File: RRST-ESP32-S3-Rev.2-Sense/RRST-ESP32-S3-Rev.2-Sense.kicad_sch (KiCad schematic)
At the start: 35 parts, among them J1 USB_C_Receptacle_USB2.0_16P, J4 Conn_01x05_Socket, J5 Conn_01x02_Socket, J6 Conn_01x02_Socket, SW1 SW_Push, SW2 SW_Push, U1 LD1117S33TR_SOT223, U2 ESP32-S3-WROOM-1, U3 MCP2561-E-SN

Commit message: 自動配線前
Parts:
- removed CAN_BUS1, CAN_BUS2: Conn_01x04_Socket, Connector_JST:JST_GH_SM04B-GHS-TB_1x04-1MP_P1.25mm_Horizontal, symbol Connector:Conn_01x04_Socket
- removed J4: Conn_01x05_Socket, Connector_PinSocket_2.54mm:PinSocket_1x05_P2.54mm_Horizontal, symbol Connector:Conn_01x05_Socket
- removed J5, J6: Conn_01x02_Socket, Connector_JST:JST_PH_S2B-PH-K_1x02_P2.00mm_Horizontal, symbol Connector:Conn_01x02_Socket
- removed U3: MCP2561-E-SN, Package_SO:SOIC-8_3.9x4.9mm_P1.27mm, symbol Interface_CAN_LIN:MCP2561-E-SN
- added J1, J3: Conn_01x22_Pin, Connector_PinHeader_2.54mm:PinHeader_1x22_P2.54mm_Vertical, symbol Connector:Conn_01x22_Pin
- added J5, J6: Conn_01x04_Socket, Connector_JST:JST_XH_B4B-XH-A_1x04_P2.50mm_Vertical, symbol Connector:Conn_01x04_Socket
- added U4: MCP2561-E-SN, Package_SO:SOIC-8_3.9x4.9mm_P1.27mm, symbol Interface_CAN_LIN:MCP2561-E-SN
- R8: footprint Resistor_SMD:R_0603_1608Metric -> Resistor_SMD:R_0805_2012Metric
- renumbered C4 to C1, C7 to C2, C8 to C3, C9 to C4, C3 to C5, C2 to C7, C5 to C8, C1 to C9, D7 to D1, D1 to D2, D2 to D3, D3 to D4, D4 to D5, D5 to D6, D6 to D8, J1 to J2, R2 to R1, R3 to R2, R4 to R3, R5 to R4, R1 to R5, U2 to U1, U1 to U2
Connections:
- net IO2 is gone; now on net CAN_TX: U1.38 (IO2)
- net IO3 is gone; now on net CAN_RX: U1.15 (IO3)
- net +3.3V: now also J1.1 (Pin_1), J1.2 (Pin_2)
- net +5V: now also J1.21 (Pin_21), J5.1 (Pin_1), J6.1 (Pin_1)
- net 5V0: now also U4.3 (VDD)
- net CANH: now also U4.7 (CANH)
- net CANL: now also U4.6 (CANL)
- net CAN_RX: now also J1.13 (Pin_13), J5.4 (Pin_4), J6.4 (Pin_4), U4.4 (RXD)
- net CAN_TX: now also J3.5 (Pin_5), J5.3 (Pin_3), J6.3 (Pin_3), U4.1 (TXD)
- net DN: now also J3.20 (Pin_20)
- net DP: now also J3.19 (Pin_19)
- net EN: now also J1.3 (Pin_3)
- net GND: now also J1.22 (Pin_22), J3.1 (Pin_1), J3.21 (Pin_21), J3.22 (Pin_22), J5.2 (Pin_2), J6.2 (Pin_2), U4.2 (VSS), U4.8 (STBY)
- net IO0: now also J3.14 (Pin_14)
- net IO1: now also J3.4 (Pin_4)
- net IO10: now also J1.16 (Pin_16)
- net IO11: now also J1.17 (Pin_17)
- net IO12: now also J1.18 (Pin_18)
- net IO13: now also J1.19 (Pin_19)
- net IO14: now also J1.20 (Pin_20)
- net IO15: now also J1.8 (Pin_8)
- net IO16: now also J1.9 (Pin_9)
- net IO17: now also J1.10 (Pin_10)
- net IO18: now also J1.11 (Pin_11)
- net IO21: now also J3.18 (Pin_18)
- net IO35: now also J3.13 (Pin_13)
- net IO36: now also J3.12 (Pin_12)
- net IO37: now also J3.11 (Pin_11)
- net IO38: now also J3.10 (Pin_10)
- net IO39: now also J3.9 (Pin_9)
- net IO4: now also J1.4 (Pin_4)
- net IO40: now also J3.8 (Pin_8)
- net IO41: now also J3.7 (Pin_7)
- net IO42: now also J3.6 (Pin_6)
- net IO45: now also J3.15 (Pin_15)
- net IO46: now also J1.14 (Pin_14)
- net IO47: now also J3.17 (Pin_17)
- net IO48: now also J3.16 (Pin_16)
- net IO5: now also J1.5 (Pin_5)
- net IO6: now also J1.6 (Pin_6)
- net IO7: now also J1.7 (Pin_7)
- net IO8: now also J1.12 (Pin_12)
- net IO9: now also J1.15 (Pin_15)
- net RXD0: now also J3.3 (Pin_3)
- net TXD0: now also J3.2 (Pin_2)
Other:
- note removed: "ピン割り当て"

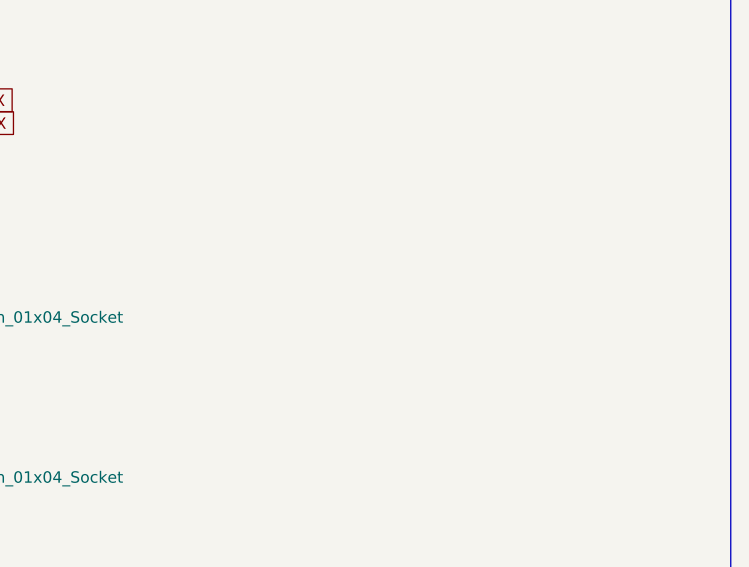
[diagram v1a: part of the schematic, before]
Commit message: 自動配線&未配線の手直し完了
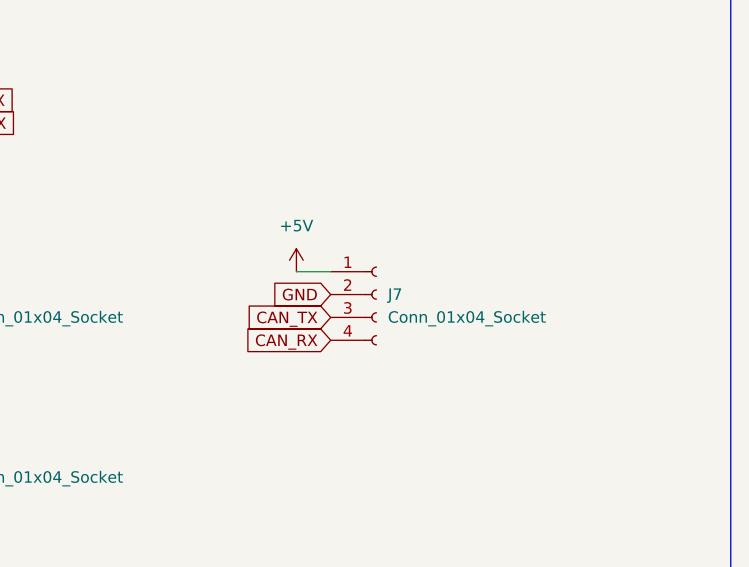
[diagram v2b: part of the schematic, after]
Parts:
- added J7: Conn_01x04_Socket, Connector_PinHeader_2.54mm:PinHeader_1x04_P2.54mm_Vertical, symbol Connector:Conn_01x04_Socket
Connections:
- net +5V: now also J7.1 (Pin_1)
- net CAN_RX: now also J7.4 (Pin_4)
- net CAN_TX: now also J7.3 (Pin_3)
- net GND: now also J7.2 (Pin_2)
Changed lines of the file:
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@@
 	(wire
 		(pts
+			(xy 332.74 128.27) (xy 336.55 128.27)
+		)
+		(stroke
+			(width 0)
+			(type default)
+		)
+	)
+	(wire
+		(pts
 			(xy 31.75 157.48) (xy 36.83 157.48)
 		)
@@
 		)
 	)
+	(global_label "CAN_RX"
+		(shape input)
+		(at 336.55 135.89 180)
+		(fields_autoplaced yes)
+		(effects
+			(font
+				(size 1.27 1.27)
+			)
+			(justify right)
+		)
+		(property "Intersheetrefs" "${INTERSHEET_REFS}"
+			(at 326.4286 135.89 0)
+			(hide yes)
+			(show_name no)
+			(do_not_autoplace no)
+			(effects
+				(font
+					(size 1.27 1.27)
+				)
+				(justify right)
+			)
+		)
+	)
 	(global_label "CANH"
 		(shape input)
@@
 		)
 	)
+	(global_label "GND"
+		(shape input)
+		(at 336.55 130.81 180)
+		(fields_autoplaced yes)
+		(effects
+			(font
+				(size 1.27 1.27)
+			)
+			(justify right)
+		)
+		(property "Intersheetrefs" "${INTERSHEET_REFS}"
+			(at 329.6943 130.81 0)
+			(hide yes)
+			(show_name no)
+			(do_not_autoplace no)
+			(effects
+				(font
+					(size 1.27 1.27)
+				)
+				(justify right)
+			)
+		)
+	)
 	(global_label "EN"
 		(shape input)
@@
 		)
 	)
+	(global_label "CAN_TX"
+		(shape input)
+		(at 336.55 133.35 180)
+		(fields_autoplaced yes)
+		(effects
+			(font
+				(size 1.27 1.27)
+			)
+			(justify right)
+		)
+		(property "Intersheetrefs" "${INTERSHEET_REFS}"
+			(at 326.731 133.35 0)
+			(hide yes)
+			(show_name no)
+			(do_not_autoplace no)
+			(effects
+				(font
+					(size 1.27 1.27)
+				)
+				(justify right)
+			)
+		)
+	)
 	(global_label "IO38"
 		(shape input)
@@
 	)
 	(symbol
+		(lib_id "power:+5V")
+		(at 332.74 128.27 0)
+		(unit 1)
+		(body_style 1)
+		(exclude_from_sim no)
+		(in_bom yes)
+		(on_board yes)
+		(in_pos_files yes)
+		(dnp no)
+		(fields_autoplaced yes)
+		(property "Reference" "#PWR026"
+			(at 332.74 132.08 0)
+			(hide yes)
+			(show_name no)
+			(do_not_autoplace no)
+			(effects
+				(font
+					(size 1.27 1.27)
+				)
+			)
+		)
+		(property "Value" "+5V"
+			(at 332.74 123.19 0)
+			(show_name no)
+			(do_not_autoplace no)
+			(effects
+				(font
+					(size 1.27 1.27)
+				)
+			)
+		)
+		(property "Footprint" ""
+			(at 332.74 128.27 0)
+			(hide yes)
+			(show_name no)
+			(do_not_autoplace no)
+			(effects
+				(font
+					(size 1.27 1.27)
+				)
+			)
+		)
+		(property "Datasheet" ""
+			(at 332.74 128.27 0)
+			(hide yes)
+			(show_name no)
+			(do_not_autoplace no)
+			(effects
+				(font
+					(size 1.27 1.27)
+				)
+			)
+		)
+		(property "Description" "Power symbol creates a global label with name \"+5V\""
+			(at 332.74 128.27 0)
+			(hide yes)
+			(show_name no)
+			(do_not_autoplace no)
+			(effects
+				(font
+					(size 1.27 1.27)
+				)
+			)
+		)
+		(pin "1"
+		)
+		(instances
+			(project "RRST-ESP32-S3-Rev.2-Sense"
+				(path "/08e3d388-f335-4566-99a5-7a0a51e9e065"
+					(reference "#PWR026")
+					(unit 1)
+				)
+			)
+		)
+	)
+	(symbol
 		(lib_id "Device:R")
 		(at 340.36 68.58 0)
@@
 					(unit 1)
 				)
+			)
+		)
+	)
+	(symbol
+		(lib_id "Connector:Conn_01x04_Socket")
+		(at 341.63 130.81 0)
+		(unit 1)
+		(body_style 1)
+		(exclude_from_sim no)
+		(in_bom yes)
+		(on_board yes)
+		(in_pos_files yes)
+		(dnp no)
+		(fields_autoplaced yes)
+		(property "Reference" "J7"
+			(at 342.9 130.8099 0)
+			(show_name no)
+			(do_not_autoplace no)
+			(effects
+				(font
+					(size 1.27 1.27)
+				)
+				(justify left)
+			)
+		)
+		(property "Value" "Conn_01x04_Socket"
+			(at 342.9 133.3499 0)
+			(show_name no)
+			(do_not_autoplace no)
+			(effects
+				(font
+					(size 1.27 1.27)
+				)
+				(justify left)
+			)
+		)
+		(property "Footprint" "Connector_PinHeader_2.54mm:PinHeader_1x04_P2.54mm_Vertical"
+			(at 341.63 130.81 0)
+			(hide yes)
+			(show_name no)
+			(do_not_autoplace no)
+			(effects
+				(font
+					(size 1.27 1.27)
+				)
+			)
+		)
+		(property "Datasheet" ""
+			(at 341.63 130.81 0)
+			(hide yes)
+			(show_name no)
+			(do_not_autoplace no)
+			(effects
+				(font
+					(size 1.27 1.27)
+				)
+			)
+		)
+		(property "Description" "Generic connector, single row, 01x04, script generated"
+			(at 341.63 130.81 0)
+			(hide yes)
+			(show_name no)
+			(do_not_autoplace no)
+			(effects
+				(font
+					(size 1.27 1.27)
+				)
+			)
+		)
+		(pin "1"
+		)
+		(pin "4"
+		)
+		(pin "3"
+		)
+		(pin "2"
+		)
+		(instances
+			(project "RRST-ESP32-S3-Rev.2-Sense"
+				(path "/08e3d388-f335-4566-99a5-7a0a51e9e065"
+					(reference "J7")
+					(unit 1)
+				)

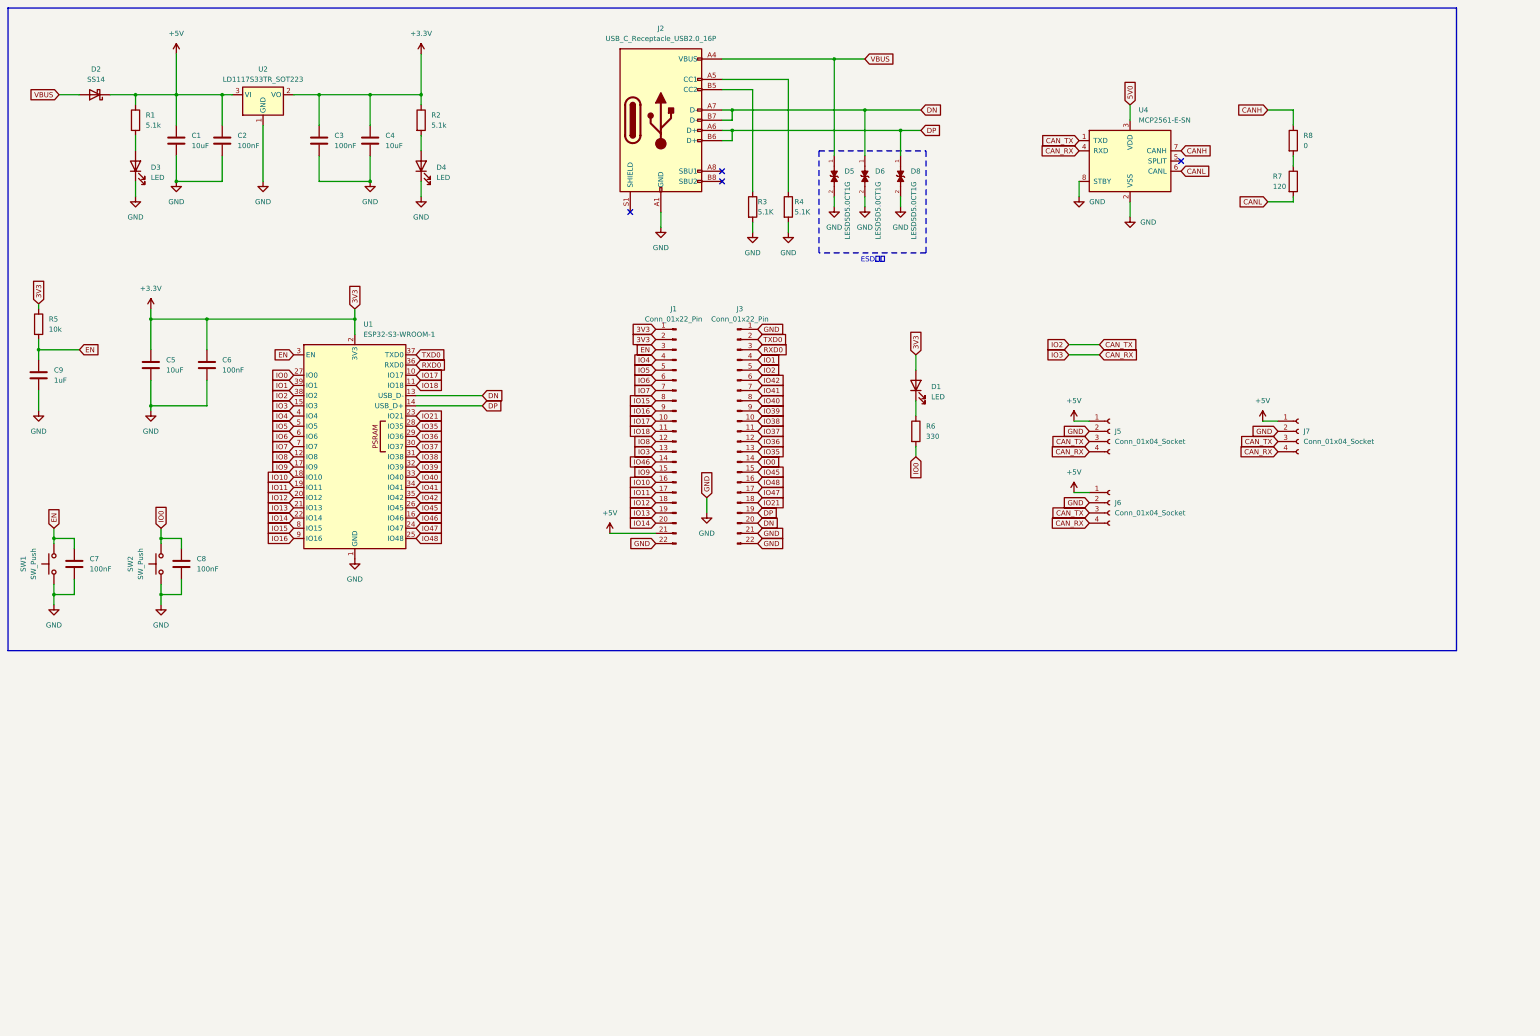
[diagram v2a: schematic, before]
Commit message: マイコンにセンサ入力を増設
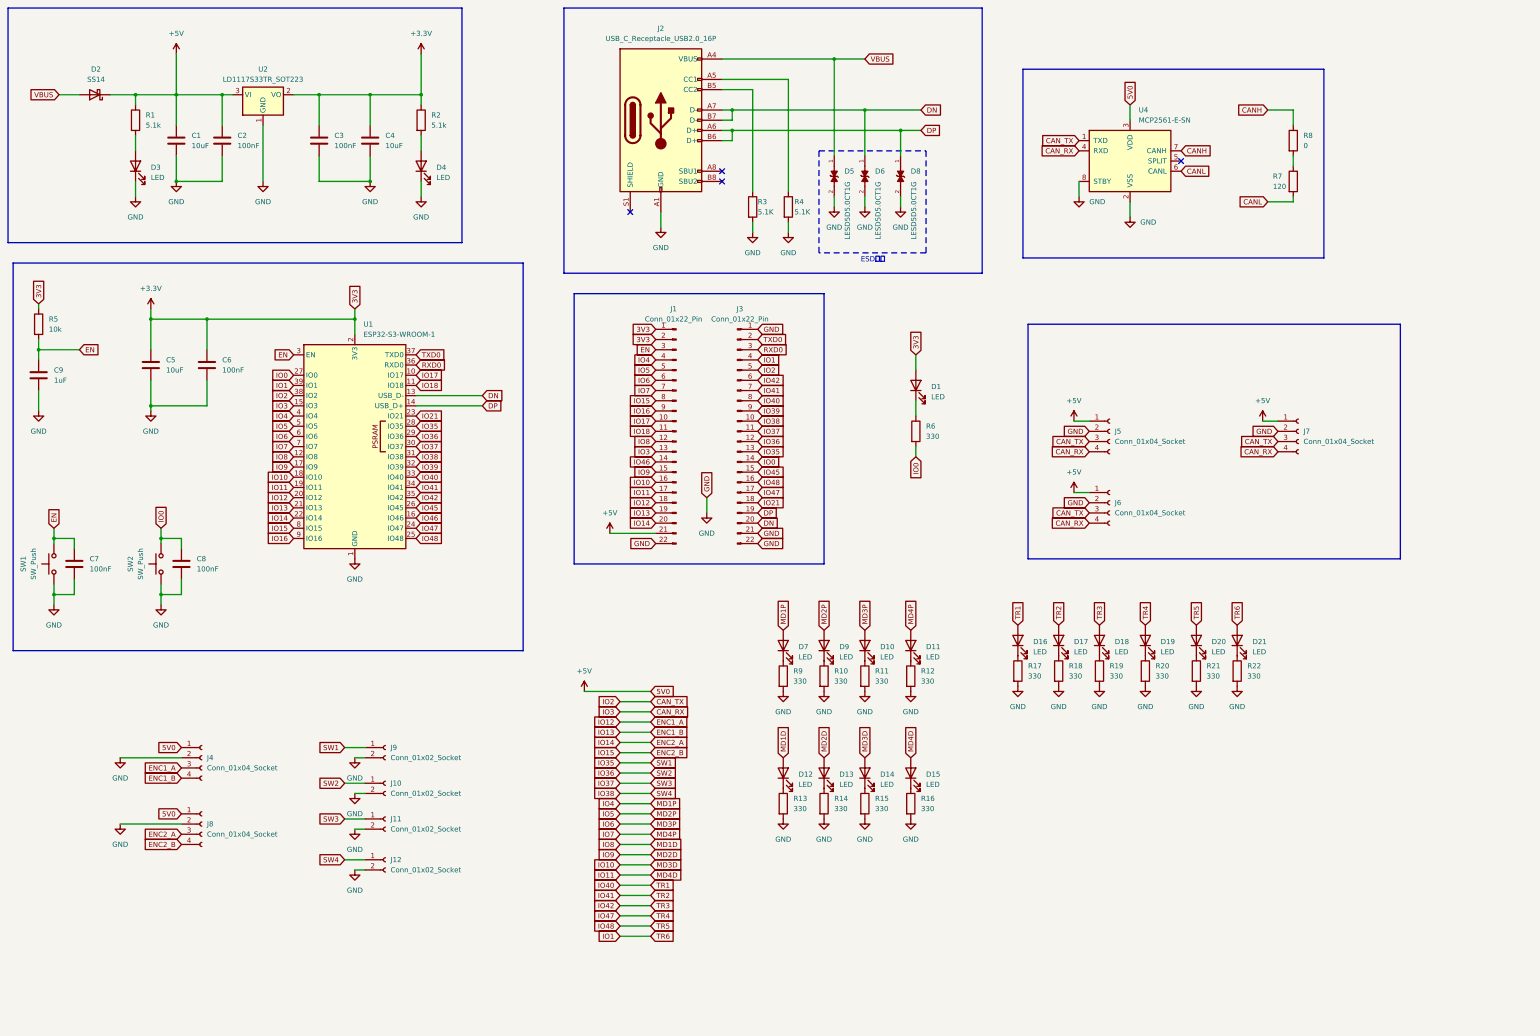
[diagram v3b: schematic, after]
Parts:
- added D10, D11, D12, D13, D14, D15, D16, D17, D18, D19, D20, D21, D7, D9: LED, LED_SMD:LED_0603_1608Metric, symbol Device:LED
- added J10, J11, J12, J9: Conn_01x02_Socket, Connector_JST:JST_XH_S2B-XH-A-1_1x02_P2.50mm_Horizontal, symbol Connector:Conn_01x02_Socket
- added J4, J8: Conn_01x04_Socket, Connector_JST:JST_XH_S4B-XH-A-1_1x04_P2.50mm_Horizontal, symbol Connector:Conn_01x04_Socket
- added R10, R11, R12, R13, R14, R15, R16, R17, R18, R19, R20, R21, R22, R9: 330, Resistor_SMD:R_0603_1608Metric, symbol Device:R
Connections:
- net 5V0 is gone; now on net +5V: U4.3 (VDD)
- net +5V: now also J4.1 (Pin_1), J8.1 (Pin_1)
- net GND: now also J10.2 (Pin_2), J11.2 (Pin_2), J12.2 (Pin_2), J4.2 (Pin_2), J8.2 (Pin_2), J9.2 (Pin_2), R10.2, R11.2, R12.2, R13.2, R14.2, R15.2, R16.2, R17.2, R18.2, R19.2, R20.2, R21.2, R22.2, R9.2
- net IO1: now also D21.2 (A)
- net IO10: now also D14.2 (A)
- net IO11: now also D15.2 (A)
- net IO35: now also J9.1 (Pin_1)
- net IO36: now also J10.1 (Pin_1)
- net IO37: now also J11.1 (Pin_1)
- net IO38: now also J12.1 (Pin_1)
- net IO4: now also D7.2 (A)
- net IO40: now also D16.2 (A)
- net IO41: now also D17.2 (A)
- net IO42: now also D18.2 (A)
- net IO47: now also D19.2 (A)
- net IO48: now also D20.2 (A)
- net IO5: now also D9.2 (A)
- net IO6: now also D10.2 (A)
- net IO7: now also D11.2 (A)
- net IO8: now also D12.2 (A)
- net IO9: now also D13.2 (A)
- net IO12 renamed ENC1_A
- net ENC1_A: now also J4.3 (Pin_3)
- net IO13 renamed ENC1_B
- net ENC1_B: now also J4.4 (Pin_4)
- net IO14 renamed ENC2_A
- net ENC2_A: now also J8.3 (Pin_3)
- net IO15 renamed ENC2_B
- net ENC2_B: now also J8.4 (Pin_4)
- new net: D9.1 (K), R10.1
- new net: D15.1 (K), R16.1
- new net: D18.1 (K), R19.1
- new net: D13.1 (K), R14.1
- new net: D16.1 (K), R17.1
- new net: D12.1 (K), R13.1
- new net: D14.1 (K), R15.1
- new net: D11.1 (K), R12.1
- new net: D17.1 (K), R18.1
- new net: D21.1 (K), R22.1
- new net: D7.1 (K), R9.1
- new net: D19.1 (K), R20.1
- new net: D10.1 (K), R11.1
- new net: D20.1 (K), R21.1

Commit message: 仮配置
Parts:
- removed D10, D11, D12, D13, D14, D15, D16, D17, D18, D19, D20, D21, D7, D9: LED, LED_SMD:LED_0603_1608Metric, symbol Device:LED
- removed R10, R11, R12, R13, R14, R15, R16, R17, R18, R19, R20, R21, R22, R9: 330, Resistor_SMD:R_0603_1608Metric, symbol Device:R
- J10, J11, J12, J9: footprint Connector_JST:JST_XH_S2B-XH-A-1_1x02_P2.50mm_Horizontal -> Connector_JST:JST_XH_B2B-XH-A_1x02_P2.50mm_Vertical
- J4, J8: footprint Connector_JST:JST_XH_S4B-XH-A-1_1x04_P2.50mm_Horizontal -> Connector_JST:JST_XH_B4B-XH-A_1x04_P2.50mm_Vertical
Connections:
- net CANH: now also J5.3 (Pin_3), J6.3 (Pin_3), J7.3 (Pin_3)
- net CANL: now also J5.4 (Pin_4), J6.4 (Pin_4), J7.4 (Pin_4)
- net CAN_RX: no longer J5.4 (Pin_4), J6.4 (Pin_4), J7.4 (Pin_4)
- net CAN_TX: no longer J5.3 (Pin_3), J6.3 (Pin_3), J7.3 (Pin_3)
